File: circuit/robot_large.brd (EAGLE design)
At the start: 26 x 33 mm, 11 parts, among them M1 SERVO-FLIPPED, M2 SERVO-1, M3 SERVO-1, U1 ESP01

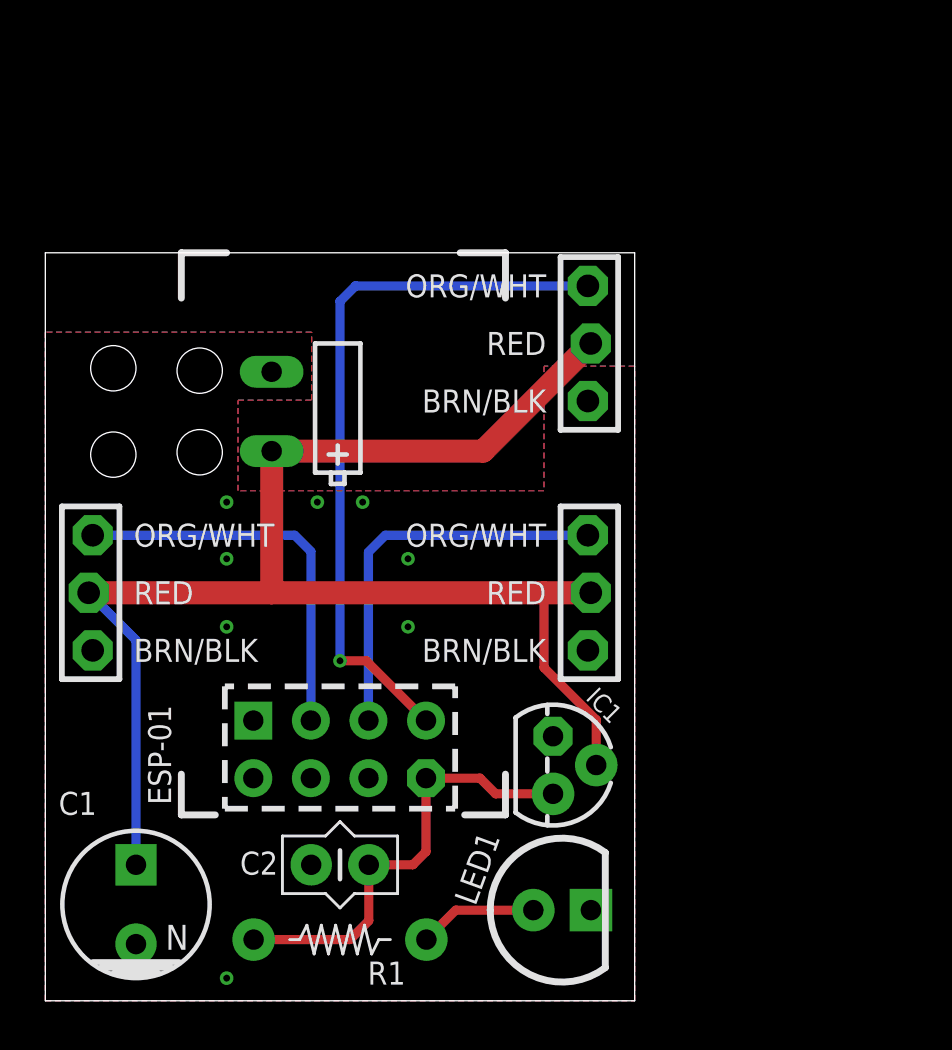
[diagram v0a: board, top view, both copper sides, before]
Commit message: smaller pcb
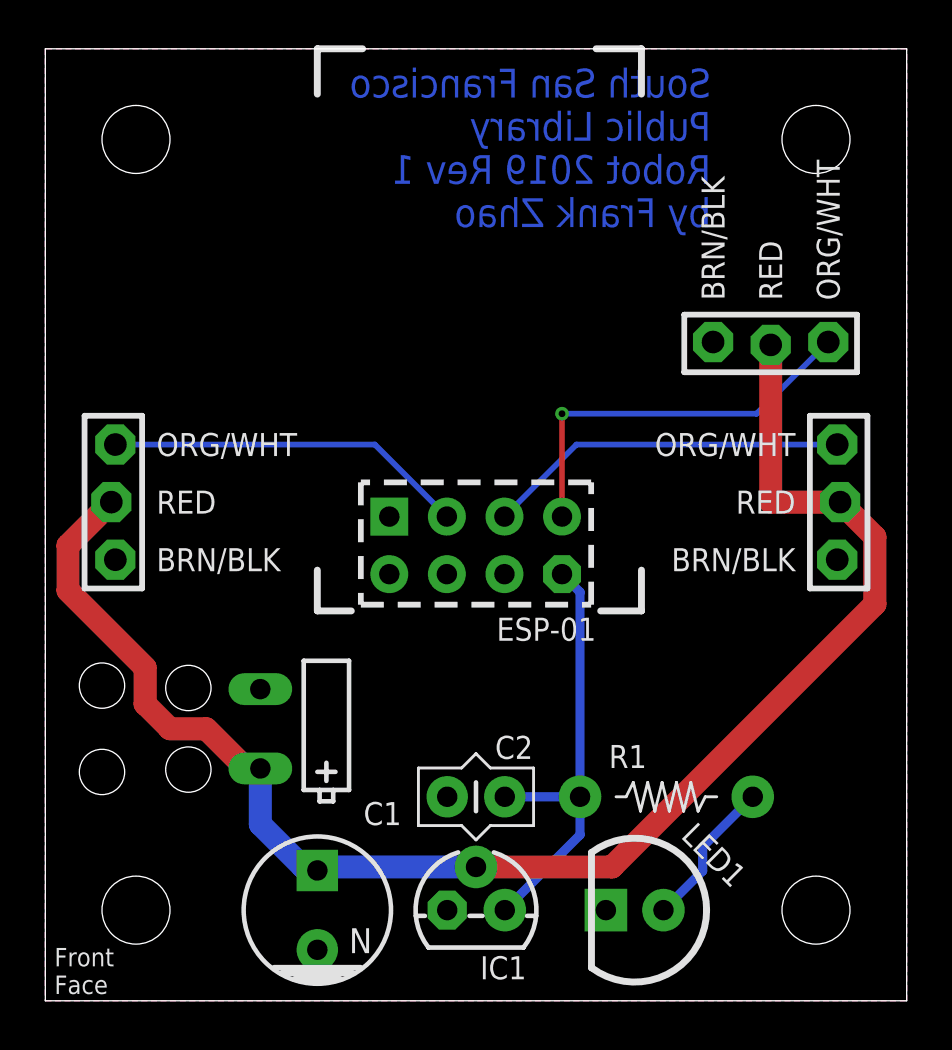
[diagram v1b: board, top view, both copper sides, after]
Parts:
- added U$10, U$11, U$12, U$13: HOLE, robot:HOLE-2MM
- U$9: value TEXT-INFO-INVISIBLE -> TEXT-INFO; device robot:TEXT-INFO-INVISIBLE -> robot:TEXT-INFO
- moved U$9 33.6 mm to (30.0, 33.5), flipped to the bottom
- moved R1 15.7 mm to (27.4, 9.00)
- moved BATTERY 14.0 mm to (2.50, 12.0)
- moved M2 11.7 mm to (35.0, 22.0)
- moved U1 10.8 mm to (19.0, 27.0)
- moved C1 8.00 mm to (12.0, 4.00)
- moved M3 8.00 mm to (32.0, 29.0), turned to 0 degrees
- moved IC1 7.25 mm to (19.0, 4.00), turned to 0 degrees
- moved C2 6.71 mm to (19.0, 9.00)
- moved M1 4.12 mm to (3.00, 22.0)
- moved LED1 3.20 mm to (26.0, 4.00), turned to 180 degrees
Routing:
- net SERVO-AUX: track 32.0 -> 17.6 mm
- net +6V: track 65.9 -> 67.8 mm
- net SERVO-LEFT: track 17.4 -> 15.9 mm
- net SERVO-RIGHT: track 17.4 -> 16.0 mm
- net N$9: track 5.26 -> 6.63 mm
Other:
- board size 26 x 33 mm -> 38 x 42 mm
- board text added: "Front Face"
- board text added: "Rear"
